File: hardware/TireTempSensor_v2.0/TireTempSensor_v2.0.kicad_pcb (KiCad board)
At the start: 4 copper layers, 27 x 54 mm, 57 parts, among them IC1 MAX15462AATA+, IC2 MLX90621ESF-BAB-000-SP, J1 SWD_01x06, J2 CAN_01x04, Q1 FQT3P20TF, SW1 RESET, U1 STM32L4P5RET6, U2 MIC5306-2.6YD5-TR, U3 SN65HVD232, Y1 16MGHz

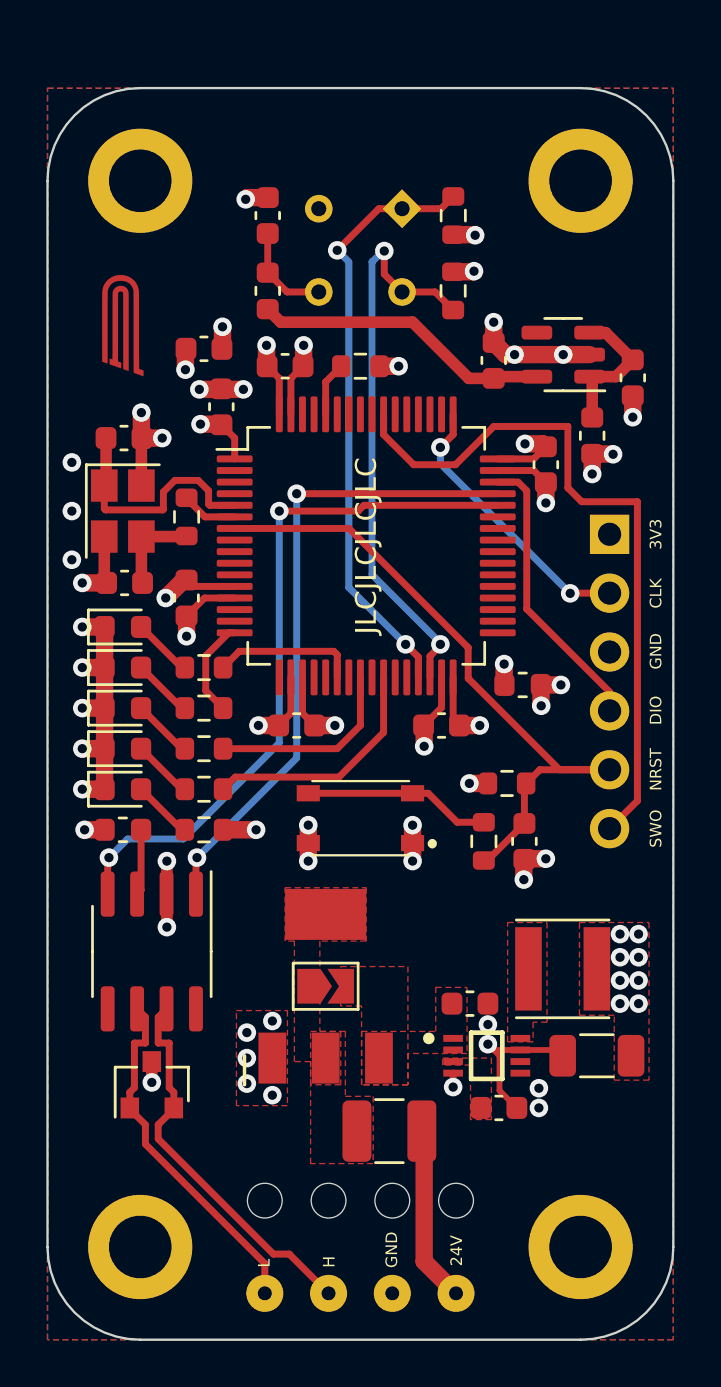
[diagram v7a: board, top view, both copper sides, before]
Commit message: footprint has been changed + some minor silkscreen changes
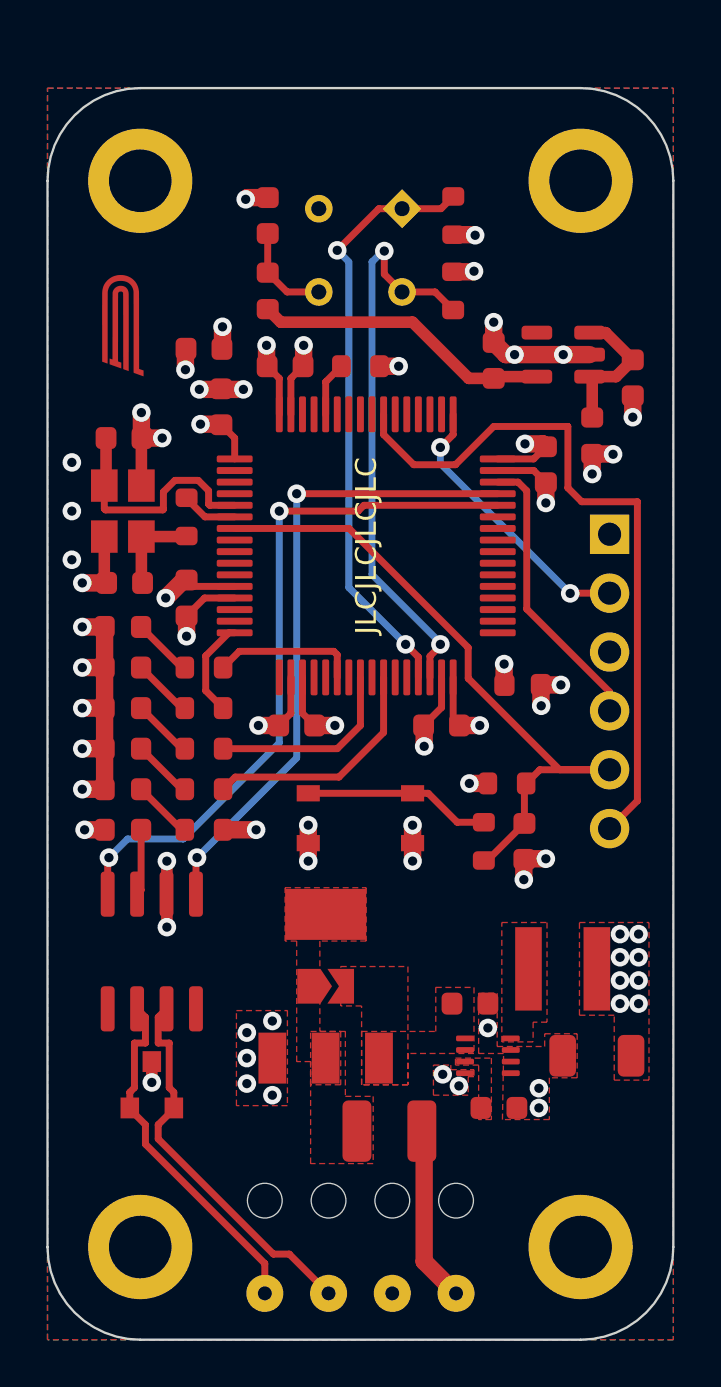
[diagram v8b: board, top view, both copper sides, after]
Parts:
- IC1: footprint BuckSyncLib:SON50P300X200X80-8N -> Package_DFN_QFN:TDFN-8-1EP_2x2mm_P0.5mm_EP0.8x1.2mm
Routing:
- net GND: track 60.9 -> 54.2 mm, vias 43 -> 42
- net +3V3: track 9.07 -> 8.47 mm, vias 18 -> 19
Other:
- board text added: "NR"
- board text removed: "NRST"
